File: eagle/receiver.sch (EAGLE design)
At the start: 15 parts, among them IC1 7805T, U1 ARDUINOR3-DIMENSION

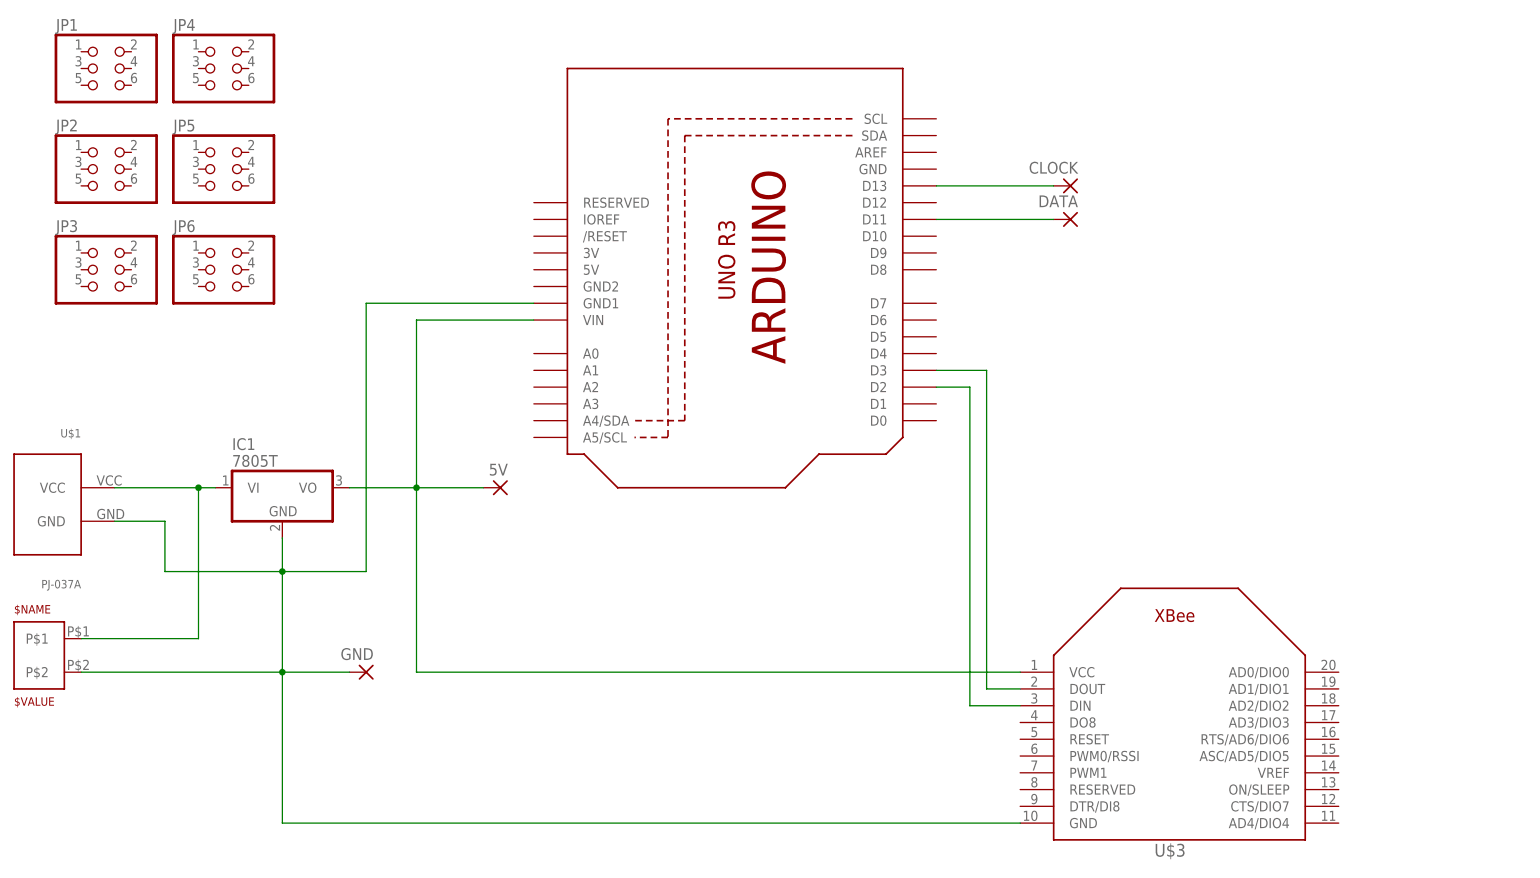
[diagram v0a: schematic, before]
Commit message: Better power management, improve usability
- LED strip pins reordered to match most strips
- Added a reset button
- Added a diode to protect the arduino from non-5vdc supplies
- Added a solder jumper to pick between sharing the arduino's 5vdc supply with
  the strip or whatever is on VCC
- Filter cap on regulator circuit
- Documentation silkscreens
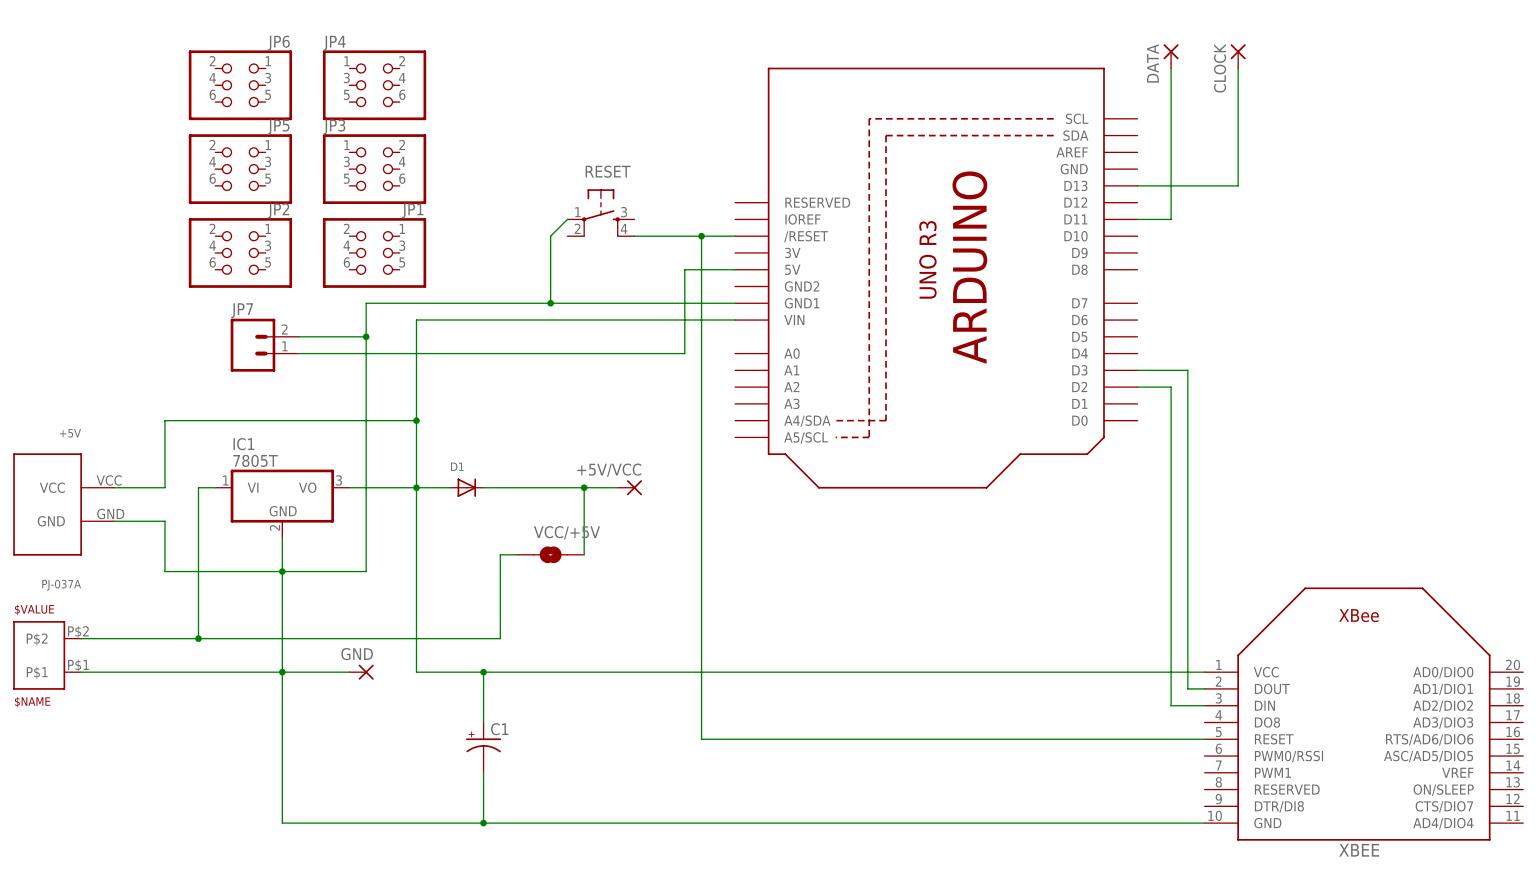
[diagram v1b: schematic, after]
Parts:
- removed 5V: (no value), wirepad:2,15/1,0
- removed U$3: XBEE, adafruit:XBEE
- added +5V/VCC: (no value), wirepad:2,15/1,0
- added C1: (no value), adafruit:CPOL-US153CLV-0405
- added D1: (no value), adafruit:DIODESMA
- added JP7: (no value), SparkFun:M02PTH
- added RESET: (no value), SparkFun:TAC_SWITCHSMD
- added VCC/+5V: NC=+5v, SparkFun:SOLDERJUMPERNO
- added XBEE: XBEE, adafruit:XBEE
- renumbered U$1 to +5V, U$2 to VCC
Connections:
- new net N$4: RESET.4, U1./RESET, XBEE.RESET
- new net N$7: JP7.1, U1.5V
- new net N$8: +5V/VCC.P, D1.C, VCC/+5V.2
- net GND: now also C1.-, JP7.2, RESET.1, VCC.P$1, XBEE.GND; no longer U$3.GND, VCC.P$2
- net N$1: now also VCC.P$2, VCC/+5V.1; no longer +5V.VCC, VCC.P$1
- net N$5: now also XBEE.DIN; no longer U$3.DIN
- net N$6: now also XBEE.DOUT; no longer U$3.DOUT
- net VCC: now also +5V.VCC, C1.+, D1.A, XBEE.VCC; no longer 5V.P, U$3.VCC
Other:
- moved on the sheet: CLOCK, DATA, JP1, JP2, JP3, JP4, JP5, JP6

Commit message: Docs++
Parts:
- C1: value (none) -> 220uF; device adafruit:CPOL-US153CLV-0405 -> phrobo:UWT0J221MCL1GB
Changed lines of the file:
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@@
 <part name="RESET" library="SparkFun" deviceset="TAC_SWITCH" device="SMD"/>
 <part name="JP7" library="SparkFun" deviceset="M02" device="PTH"/>
-<part name="C1" library="adafruit" deviceset="CPOL-US" device="153CLV-0405"/>
+<part name="C1" library="phrobo" deviceset="UWT0J221MCL1GB" device="" value="220uF"/>
 <part name="D1" library="adafruit" deviceset="DIODE" device="SMA"/>
 <part name="VCC/+5V" library="SparkFun" deviceset="SOLDERJUMPER" device="NO" value="NC=+5v"/>
@@
 <junction x="45.72" y="86.36"/>
 <pinref part="C1" gate="G$1" pin="-"/>
-<wire x1="63.5" y1="20.32" x2="63.5" y2="12.7" width="0.1524" layer="91"/>
+<wire x1="63.5" y1="22.4" x2="63.5" y2="12.7" width="0.1524" layer="91"/>
 <junction x="63.5" y="12.7"/>
 </segment>
@@
 <wire x1="53.34" y1="88.9" x2="101.6" y2="88.9" width="0.1524" layer="91"/>
 <pinref part="C1" gate="G$1" pin="+"/>
-<wire x1="63.5" y1="27.94" x2="63.5" y2="35.56" width="0.1524" layer="91"/>
+<wire x1="63.5" y1="29.4" x2="63.5" y2="35.56" width="0.1524" layer="91"/>
 <junction x="63.5" y="35.56"/>
 <pinref part="+5V" gate="G$1" pin="VCC"/>

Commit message: Unflip flipped parts
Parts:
- D1: device adafruit:DIODESMA -> adafruit:DIODESOD-323F
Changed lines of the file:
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@@
 <part name="JP7" library="SparkFun" deviceset="M02" device="PTH"/>
 <part name="C1" library="phrobo" deviceset="UWT0J221MCL1GB" device="" value="220uF"/>
-<part name="D1" library="adafruit" deviceset="DIODE" device="SMA"/>
+<part name="D1" library="adafruit" deviceset="DIODE" device="SOD-323F"/>
 <part name="VCC/+5V" library="SparkFun" deviceset="SOLDERJUMPER" device="NO" value="NC=+5v"/>
 </parts>
@@
 </sheet>
 </sheets>
+<errors>
+</errors>
 </schematic>
 </drawing>
